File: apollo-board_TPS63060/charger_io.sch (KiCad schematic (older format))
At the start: 16 parts, among them J2 Barrel_Jack_Switch, J3 Conn_01x02_Male, Q2 Si3421DV, U2 USB-C, U3 IP4220CZ6

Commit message: Remove unused parts at schematic level.
+ solve schematic DRC issues
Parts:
- removed J2: Barrel_Jack_Switch, Connector_BarrelJack:BarrelJack_CUI_PJ-102AH_Horizontal, symbol Connector:Barrel_Jack_Switch
- removed TP6, TP7: TestPoint, TestPoint:TestPoint_Pad_D1.0mm, symbol Connector:TestPoint
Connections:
- wire segments 57 -> 54
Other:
- note removed: "Barrel Jack\n"
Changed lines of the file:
@@
 Text Notes 4250 5750 0    50   ~ 0
 Pull-Down via 5k1\nresistor for 5V 3A PD
-$Comp
-L Connector:Barrel_Jack_Switch J2
-U 1 1 5F72FE29
-P 4200 3000
-F 0 "J2" H 4257 3317 50  0000 C CNN
-F 1 "Barrel_Jack_Switch" H 4257 3226 50  0000 C CNN
-F 2 "Connector_BarrelJack:BarrelJack_CUI_PJ-102AH_Horizontal" H 4250 2960 50  0001 C CNN
-F 3 "~" H 4250 2960 50  0001 C CNN
-	1    4200 3000
-	1    0    0    -1
-$EndComp
-$Comp
-L power:GND #PWR018
-U 1 1 5F731685
-P 4600 3200
-F 0 "#PWR018" H 4600 2950 50  0001 C CNN
-F 1 "GND" H 4605 3027 50  0000 C CNN
-F 2 "" H 4600 3200 50  0001 C CNN
-F 3 "" H 4600 3200 50  0001 C CNN
-	1    4600 3200
-	1    0    0    -1
-$EndComp
-Wire Wire Line
-	4600 3200 4600 3100
-Wire Wire Line
-	4600 3000 4500 3000
-Wire Wire Line
-	4500 3100 4600 3100
-Connection ~ 4600 3100
-Wire Wire Line
-	4600 3100 4600 3000
-Wire Wire Line
-	4500 2900 4950 2900
-Text Label 4950 2900 2    50   ~ 0
-V_CHARGE
 Text Label 7400 3050 2    50   ~ 0
 V_CHARGE
@@
 Wire Wire Line
 	7200 3250 7200 3150
-Text Notes 3350 2250 0    50   ~ 10
-Barrel Jack\n
 Text Notes 5900 2250 0    50   ~ 10
 External Input Pads
@@
 Wire Wire Line
 	1950 1250 1300 1250
-Wire Notes Line
-	3250 4050 3250 2100
 Wire Notes Line
 	5800 2100 5800 7450
@@
 Wire Wire Line
 	2050 6950 2050 7050
-Text Notes 3250 4800 0    50   ~ 0
+Text Notes 3500 4900 0    50   ~ 0
 So you can disable \nVBUS if you only \nneed data\n(5V will have to\nbe provided to\nVBUS)\n
 Text Label 5250 6800 2    50   ~ 0
@@
 F 3 "~" H 2150 1250 50  0001 C CNN
 	1    1950 1250
-	0    1    1    0
-$EndComp
-$Comp
-L Connector:TestPoint TP6
-U 1 1 5FD7785B
-P 1950 1550
-F 0 "TP6" V 1904 1738 50  0000 L CNN
-F 1 "TestPoint" V 1995 1738 50  0000 L CNN
-F 2 "TestPoint:TestPoint_Pad_D1.0mm" H 2150 1550 50  0001 C CNN
-F 3 "~" H 2150 1550 50  0001 C CNN
-	1    1950 1550
-	0    1    1    0
-$EndComp
-$Comp
-L Connector:TestPoint TP7
-U 1 1 5FD77B2F
-P 1950 1750
-F 0 "TP7" V 1904 1938 50  0000 L CNN
-F 1 "TestPoint" V 1995 1938 50  0000 L CNN
-F 2 "TestPoint:TestPoint_Pad_D1.0mm" H 2150 1750 50  0001 C CNN
-F 3 "~" H 2150 1750 50  0001 C CNN
-	1    1950 1750
 	0    1    1    0
 $EndComp
@@
 Text Notes 5350 1300 0    118  ~ 24
 Power Voltage Range : 5-15V
-Text Notes 5000 2900 0    50   ~ 10
-<- 15V Max
 Text Notes 7450 3050 0    50   ~ 10
 <- 15V Max
 Wire Wire Line
-	3100 5050 3500 5050
+	3100 5050 3200 5050
 Wire Notes Line
 	8400 2100 8400 5800
@@
 	9250 3000 9250 2900
 Wire Notes Line
-	11050 2100 3250 2100
-Wire Notes Line
 	1100 7450 1100 4050
+Wire Notes Line
+	11050 2100 5800 2100
+$Comp
+L power:PWR_FLAG #FLG0103
+U 1 1 60345563
+P 3200 4850
+F 0 "#FLG0103" H 3200 4925 50  0001 C CNN
+F 1 "PWR_FLAG" H 3200 5023 50  0000 C CNN
+F 2 "" H 3200 4850 50  0001 C CNN
+F 3 "~" H 3200 4850 50  0001 C CNN
+	1    3200 4850
+	1    0    0    -1
+$EndComp
+Wire Wire Line
+	3200 4850 3200 5050
+Connection ~ 3200 5050
+Wire Wire Line
+	3200 5050 3500 5050
 $EndSCHEMATC

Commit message: Update USB-C receptacle symbol fields
Add Mfr Name & ref., DataSheet + Alternative Equivalent Part
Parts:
- U2: Alternative_Part_Datasheet (none) -> https://datasheet.lcsc.com/szlcsc/1811131825_Korean-Hropart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; Alternative_Part_Mfr_name (none) -> Korean Hroparts Elec; Alternative_Part_Mfr_no (none) -> TYPE-C-31-M-12; Mfr_name (none) -> Global Connector Technology; Mfr_no (none) -> USB4105-15-A
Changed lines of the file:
@@
 F 1 "USB-C" H 2100 7550 50  0000 C CNB
 F 2 "usb_c:usb-c-usb4105" H 2450 6250 50  0001 C CNN
-F 3 "" H 2450 6250 50  0001 C CNN
+F 3 "https://gct.co/files/drawings/usb4105.pdf" H 2450 6250 50  0001 C CNN
+F 4 "Global Connector Technology" H 2450 6250 50  0001 C CNN "Mfr_name"
+F 5 "USB4105-15-A" H 2450 6250 50  0001 C CNN "Mfr_no"
+F 6 "Korean Hroparts Elec" H 2450 6250 50  0001 C CNN "Alternative_Part_Mfr_name"
+F 7 "TYPE-C-31-M-12" H 2450 6250 50  0001 C CNN "Alternative_Part_Mfr_no"
+F 8 "https://datasheet.lcsc.com/szlcsc/1811131825_Korean-Hroparts-Elec-TYPE-C-31-M-12_C165948.pdf" H 2450 6250 50  0001 C CNN "Alternative_Part_Datasheet"
 	1    2450 6250
 	1    0    0    -1

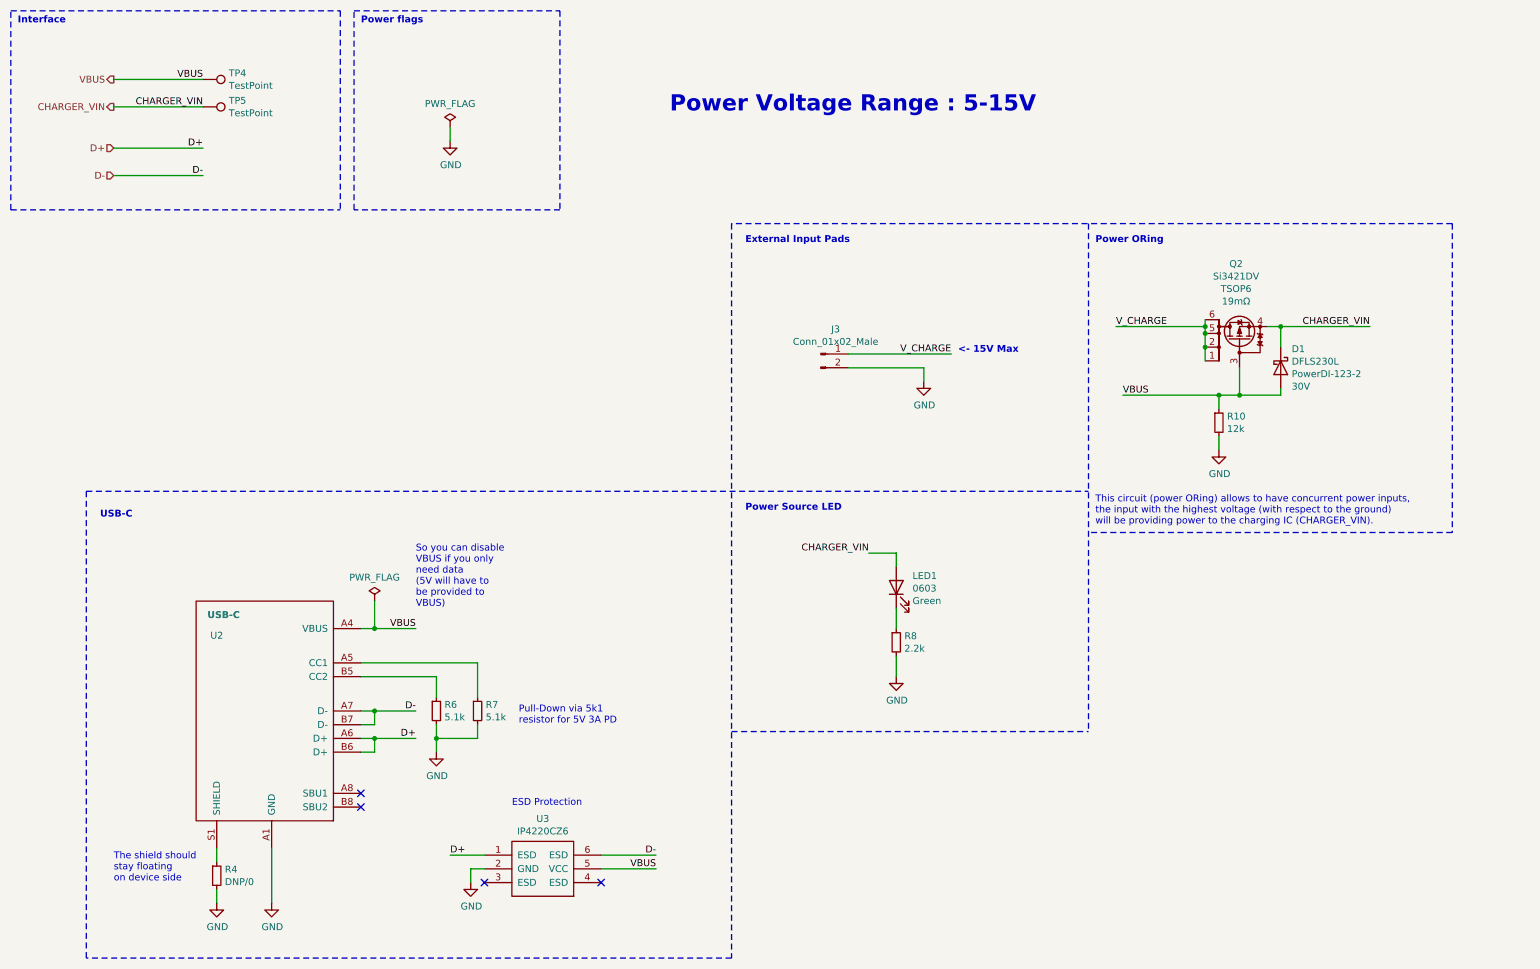
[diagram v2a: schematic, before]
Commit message: Rename some power signal on Schematic to improve readability.
+ Misc. updates
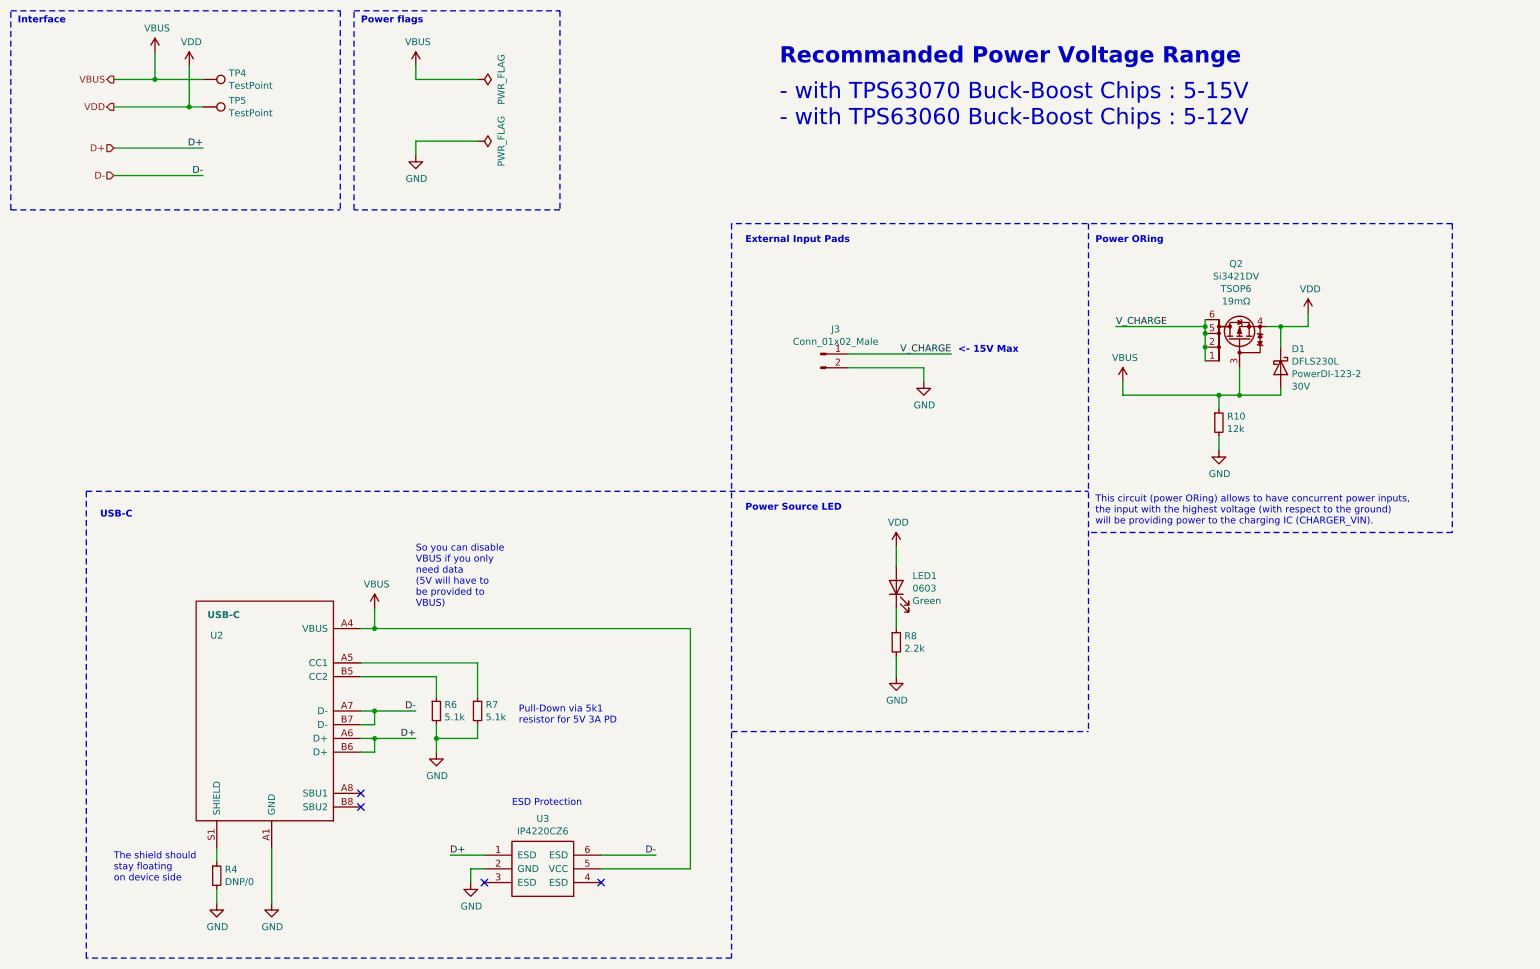
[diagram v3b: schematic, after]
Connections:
- net CHARGER_VIN renamed VDD
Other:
- note added: "- with TPS63070 Buck-Boost Chips : 5-15V\n- with TPS63060 Buck-Boost Chips : 5-12V"
- note added: "Recommanded Power Voltage Range"
- note removed: "Power Voltage Range : 5-15V"
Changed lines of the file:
@@
 VBUS
 Text HLabel 1300 1250 0    50   Output ~ 0
-CHARGER_VIN
+VDD
 Text HLabel 1300 1550 0    50   Input ~ 0
 D+
@@
 USB-C
 Wire Wire Line
-	1950 1050 1300 1050
-Wire Wire Line
-	1950 1250 1300 1250
+	1950 1250 1850 1250
 Wire Notes Line
 	5800 2100 5800 7450
@@
 Text Notes 3500 4900 0    50   ~ 0
 So you can disable \nVBUS if you only \nneed data\n(5V will have to\nbe provided to\nVBUS)\n
-Text Label 5250 6800 2    50   ~ 0
-VBUS
 Text Label 5250 6700 2    50   ~ 0
 D-
@@
 Wire Wire Line
 	9350 3350 9350 3450
-Text Label 10450 2850 2    50   ~ 0
-CHARGER_VIN
 Text Label 8600 2850 0    50   ~ 0
 V_CHARGE
@@
 Text Notes 8450 4300 0    50   ~ 0
 This circuit (power ORing) allows to have concurrent power inputs,\nthe input with the highest voltage (with respect to the ground)\nwill be providing power to the charging IC (CHARGER_VIN).
-Text Label 1950 1250 2    50   ~ 0
-CHARGER_VIN
 $Comp
 L Device:R_Small R?
@@
 Wire Wire Line
 	7000 5250 7000 5400
-Wire Wire Line
-	7000 4600 7000 4500
-Wire Wire Line
-	7000 4500 6800 4500
-Text Label 6800 4500 2    50   ~ 0
-CHARGER_VIN
 Text Notes 5900 4200 0    50   ~ 10
 Power Source LED
@@
 	0    1    1    0
 $EndComp
-Text Notes 5350 1300 0    118  ~ 24
-Power Voltage Range : 5-15V
+Text Notes 6150 950  0    118  ~ 24
+Recommanded Power Voltage Range
 Text Notes 7450 3050 0    50   ~ 10
 <- 15V Max
@@
 L power:GND #PWR0106
 U 1 1 5FE186B3
-P 3750 1500
-F 0 "#PWR0106" H 3750 1250 50  0001 C CNN
-F 1 "GND" H 3755 1327 50  0000 C CNN
-F 2 "" H 3750 1500 50  0001 C CNN
-F 3 "" H 3750 1500 50  0001 C CNN
-	1    3750 1500
+P 3500 1600
+F 0 "#PWR0106" H 3500 1350 50  0001 C CNN
+F 1 "GND" H 3505 1427 50  0000 C CNN
+F 2 "" H 3500 1600 50  0001 C CNN
+F 3 "" H 3500 1600 50  0001 C CNN
+	1    3500 1600
 	1    0    0    -1
 $EndComp
@@
 L power:PWR_FLAG #FLG0101
 U 1 1 5FE193A0
-P 3750 1400
-F 0 "#FLG0101" H 3750 1475 50  0001 C CNN
-F 1 "PWR_FLAG" H 3750 1573 50  0000 C CNN
-F 2 "" H 3750 1400 50  0001 C CNN
-F 3 "~" H 3750 1400 50  0001 C CNN
-	1    3750 1400
-	1    0    0    -1
-$EndComp
-Wire Wire Line
-	3750 1400 3750 1500
+P 3950 1500
+F 0 "#FLG0101" H 3950 1575 50  0001 C CNN
+F 1 "PWR_FLAG" H 3950 1673 50  0000 C CNN
+F 2 "" H 3950 1500 50  0001 C CNN
+F 3 "~" H 3950 1500 50  0001 C CNN
+	1    3950 1500
+	0    1    1    0
+$EndComp
 Wire Notes Line
 	3050 550  4550 550
@@
 	4850 6700 5250 6700
 Wire Wire Line
-	4850 6800 5250 6800
-Text Label 3500 5050 2    50   ~ 0
-VBUS
-Text Label 8650 3350 0    50   ~ 0
-VBUS
-Text Label 1950 1050 2    50   ~ 0
-VBUS
-Wire Wire Line
 	8600 2850 9250 2850
 Wire Wire Line
@@
 Connection ~ 9800 2850
 Wire Wire Line
-	9800 2850 10450 2850
+	9800 2850 10000 2850
 Wire Wire Line
 	9250 2900 9250 2850
@@
 Wire Notes Line
 	11050 2100 5800 2100
+Wire Wire Line
+	3200 4900 3200 5050
+$Comp
+L power:VDD #PWR0119
+U 1 1 610F5550
+P 7000 4450
+F 0 "#PWR0119" H 7000 4300 50  0001 C CNN
+F 1 "VDD" H 7015 4623 50  0000 C CNN
+F 2 "" H 7000 4450 50  0001 C CNN
+F 3 "" H 7000 4450 50  0001 C CNN
+	1    7000 4450
+	1    0    0    -1
+$EndComp
+$Comp
+L power:VDD #PWR0120
+U 1 1 610F5B4F
+P 10000 2750
+F 0 "#PWR0120" H 10000 2600 50  0001 C CNN
+F 1 "VDD" H 10015 2923 50  0000 C CNN
+F 2 "" H 10000 2750 50  0001 C CNN
+F 3 "" H 10000 2750 50  0001 C CNN
+	1    10000 2750
+	1    0    0    -1
+$EndComp
+Wire Wire Line
+	10000 2750 10000 2850
+Wire Wire Line
+	7000 4450 7000 4600
+Wire Wire Line
+	1950 1050 1600 1050
+$Comp
+L power:VDD #PWR0121
+U 1 1 610F6055
+P 1850 950
+F 0 "#PWR0121" H 1850 800 50  0001 C CNN
+F 1 "VDD" H 1865 1123 50  0000 C CNN
+F 2 "" H 1850 950 50  0001 C CNN
+F 3 "" H 1850 950 50  0001 C CNN
+	1    1850 950
+	1    0    0    -1
+$EndComp
+Wire Wire Line
+	1850 950  1850 1250
+Connection ~ 1850 1250
+Wire Wire Line
+	1850 1250 1300 1250
+$Comp
+L power:VBUS #PWR0122
+U 1 1 61100595
+P 3500 950
+F 0 "#PWR0122" H 3500 800 50  0001 C CNN
+F 1 "VBUS" H 3515 1123 50  0000 C CNN
+F 2 "" H 3500 950 50  0001 C CNN
+F 3 "" H 3500 950 50  0001 C CNN
+	1    3500 950
+	1    0    0    -1
+$EndComp
+$Comp
+L power:VBUS #PWR0123
+U 1 1 61100F37
+P 1600 850
+F 0 "#PWR0123" H 1600 700 50  0001 C CNN
+F 1 "VBUS" H 1615 1023 50  0000 C CNN
+F 2 "" H 1600 850 50  0001 C CNN
+F 3 "" H 1600 850 50  0001 C CNN
+	1    1600 850
+	1    0    0    -1
+$EndComp
+Wire Wire Line
+	1600 850  1600 1050
+Connection ~ 1600 1050
+Wire Wire Line
+	1600 1050 1300 1050
+$Comp
+L power:VBUS #PWR0124
+U 1 1 61102547
+P 3200 4900
+F 0 "#PWR0124" H 3200 4750 50  0001 C CNN
+F 1 "VBUS" H 3215 5073 50  0000 C CNN
+F 2 "" H 3200 4900 50  0001 C CNN
+F 3 "" H 3200 4900 50  0001 C CNN
+	1    3200 4900
+	1    0    0    -1
+$EndComp
 $Comp
 L power:PWR_FLAG #FLG0103
 U 1 1 60345563
-P 3200 4850
-F 0 "#FLG0103" H 3200 4925 50  0001 C CNN
-F 1 "PWR_FLAG" H 3200 5023 50  0000 C CNN
-F 2 "" H 3200 4850 50  0001 C CNN
-F 3 "~" H 3200 4850 50  0001 C CNN
-	1    3200 4850
-	1    0    0    -1
-$EndComp
-Wire Wire Line
-	3200 4850 3200 5050
+P 3950 1050
+F 0 "#FLG0103" H 3950 1125 50  0001 C CNN
+F 1 "PWR_FLAG" H 3950 1223 50  0000 C CNN
+F 2 "" H 3950 1050 50  0001 C CNN
+F 3 "~" H 3950 1050 50  0001 C CNN
+	1    3950 1050
+	0    1    1    0
+$EndComp
+Wire Wire Line
+	5500 6800 5500 5050
+Wire Wire Line
+	5500 5050 3200 5050
+Wire Wire Line
+	4850 6800 5500 6800
 Connection ~ 3200 5050
-Wire Wire Line
-	3200 5050 3500 5050
+$Comp
+L power:VBUS #PWR0125
+U 1 1 611108B5
+P 8650 3250
+F 0 "#PWR0125" H 8650 3100 50  0001 C CNN
+F 1 "VBUS" H 8665 3423 50  0000 C CNN
+F 2 "" H 8650 3250 50  0001 C CNN
+F 3 "" H 8650 3250 50  0001 C CNN
+	1    8650 3250
+	1    0    0    -1
+$EndComp
+Wire Wire Line
+	8650 3250 8650 3350
+Wire Wire Line
+	3500 950  3500 1050
+Wire Wire Line
+	3500 1050 3950 1050
+Wire Wire Line
+	3950 1500 3500 1500
+Wire Wire Line
+	3500 1500 3500 1600
+Text Notes 6150 1400 0    118  ~ 0
+- with TPS63070 Buck-Boost Chips : 5-15V\n- with TPS63060 Buck-Boost Chips : 5-12V
 $EndSCHEMATC
